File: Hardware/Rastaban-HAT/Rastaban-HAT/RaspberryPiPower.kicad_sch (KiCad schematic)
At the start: 11 parts, among them IC2 BCM53DS, Q3 DMG2305UX-7, U5 LM2596S -5.0

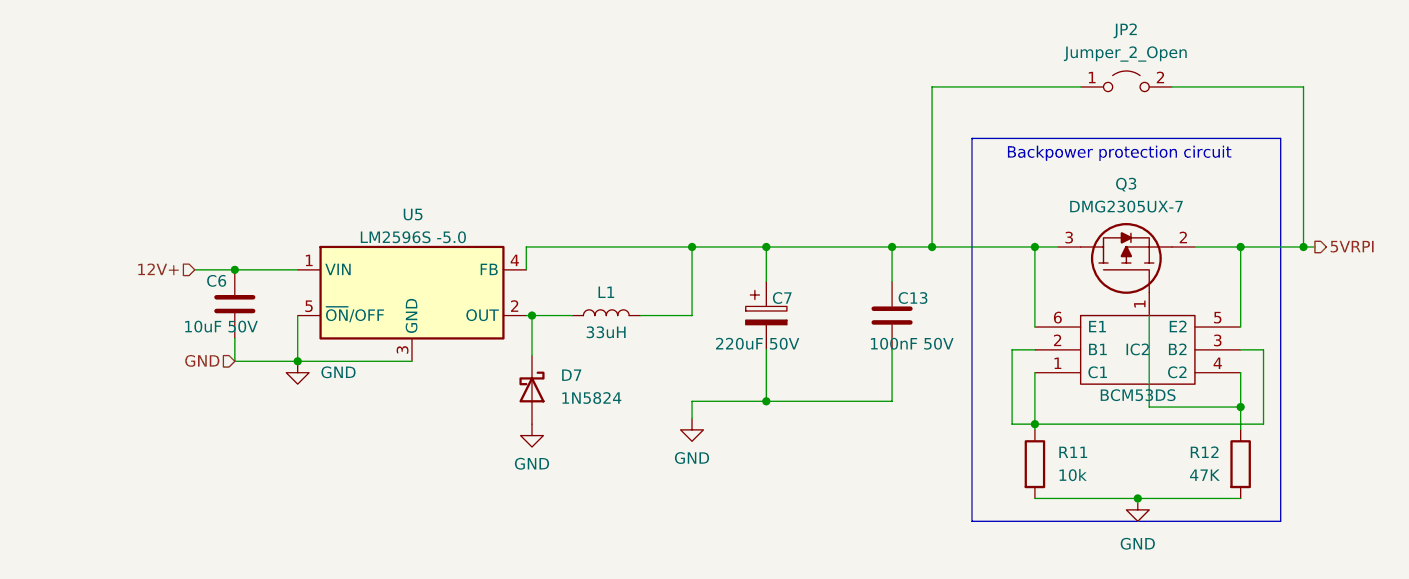
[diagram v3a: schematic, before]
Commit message: improved RPI Power circuit
-added capacitors and values
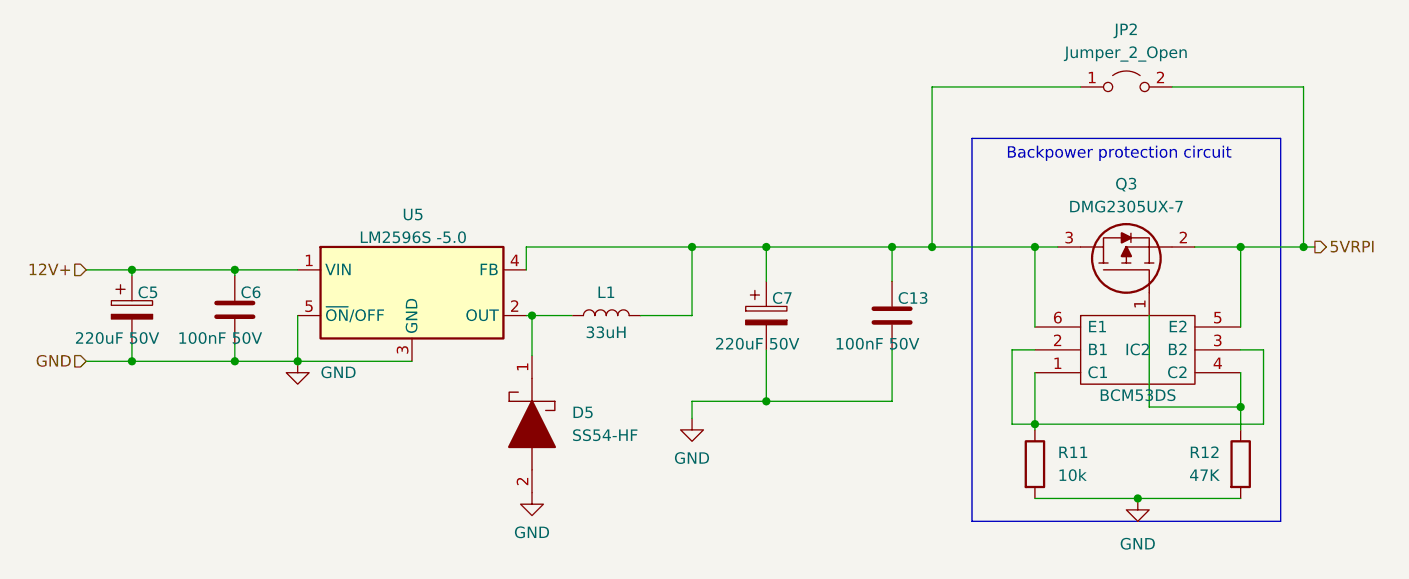
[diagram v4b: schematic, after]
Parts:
- removed D7: 1N5824, SamacSys_Parts:SOD2512X110N, symbol Device:D_Schottky
- added C5: 220uF 50V, Capacitor_SMD:CP_Elec_8x10, symbol Device:C_Polarized
- added D5: SS54-HF, DIOM5025X220N, symbol SamacSys_Parts:SS54-HF
- C6: value 10uF 50V -> 100nF 50V
- L1: footprint Inductor_SMD:L_Bourns-SRU8028_8.0x8.0mm -> Inductor_SMD:L_Bourns_SRR1208_12.7x12.7mm
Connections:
- net 12V+: now also C5.1
- net GND: now also C5.2, D5.2
- net at L1.1, U5.2 (OUT): now also D5.1
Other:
- moved on the sheet: C6
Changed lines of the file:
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@@
   (junction (at 50.165 60.96) (diameter 0) (color 0 0 0 0)
   )
+  (junction (at 38.735 60.96) (diameter 0) (color 0 0 0 0)
+  )
   (junction (at 100.965 58.42) (diameter 0) (color 0 0 0 0)
   )
@@
   (junction (at 127.635 58.42) (diameter 0) (color 0 0 0 0)
   )
+  (junction (at 50.165 71.12) (diameter 0) (color 0 0 0 0)
+  )
   (junction (at 83.185 66.04) (diameter 0) (color 0 0 0 0)
   )
+  (junction (at 38.735 71.12) (diameter 0) (color 0 0 0 0)
+  )
   (junction (at 109.22 58.42) (diameter 0) (color 0 0 0 0)
   )
@@
     (stroke (width 0) (type default) (color 0 0 0 0))
   )
-  (wire (pts (xy 50.165 68.58) (xy 50.165 71.12))
+  (wire (pts (xy 50.165 69.215) (xy 50.165 71.12))
     (stroke (width 0) (type default) (color 0 0 0 0))
   )
@@
     (stroke (width 0) (type default) (color 0 0 0 0))
   )
+  (wire (pts (xy 50.165 61.595) (xy 50.165 60.96))
+    (stroke (width 0) (type default) (color 0 0 0 0))
+  )
   (wire (pts (xy 139.065 58.42) (xy 139.065 67.31))
     (stroke (width 0) (type default) (color 0 0 0 0))
@@
     (stroke (width 0) (type default) (color 0 0 0 0))
   )
+  (wire (pts (xy 38.735 69.215) (xy 38.735 71.12))
+    (stroke (width 0) (type default) (color 0 0 0 0))
+  )
   (wire (pts (xy 127.635 40.64) (xy 127.635 58.42))
     (stroke (width 0) (type default) (color 0 0 0 0))
@@
     (stroke (width 0) (type default) (color 0 0 0 0))
   )
+  (wire (pts (xy 38.735 71.12) (xy 50.165 71.12))
+    (stroke (width 0) (type default) (color 0 0 0 0))
+  )
   (wire (pts (xy 109.22 69.85) (xy 109.22 75.565))
     (stroke (width 0) (type default) (color 0 0 0 0))
@@
     (stroke (width 0) (type default) (color 0 0 0 0))
   )
-  (wire (pts (xy 45.72 60.96) (xy 50.165 60.96))
+  (wire (pts (xy 38.735 60.96) (xy 50.165 60.96))
+    (stroke (width 0) (type default) (color 0 0 0 0))
+  )
+  (wire (pts (xy 33.655 60.96) (xy 38.735 60.96))
     (stroke (width 0) (type default) (color 0 0 0 0))
   )
   (wire (pts (xy 161.925 69.85) (xy 164.465 69.85))
+    (stroke (width 0) (type default) (color 0 0 0 0))
+  )
+  (wire (pts (xy 33.655 71.12) (xy 38.735 71.12))
+    (stroke (width 0) (type default) (color 0 0 0 0))
+  )
+  (wire (pts (xy 38.735 61.595) (xy 38.735 60.96))
     (stroke (width 0) (type default) (color 0 0 0 0))
   )
@@
     (effects (font (size 1.27 1.27)) (justify left))
   )
-  (hierarchical_label "12V+" (shape input) (at 45.72 60.96 180)
+  (hierarchical_label "12V+" (shape input) (at 33.655 60.96 180)
     (effects (font (size 1.27 1.27)) (justify right))
   )
-  (hierarchical_label "GND" (shape input) (at 50.165 71.12 180)
+  (hierarchical_label "GND" (shape input) (at 33.655 71.12 180)
     (effects (font (size 1.27 1.27)) (justify right))
   )
-  (symbol (lib_id "power:GND") (at 83.185 78.105 0) (unit 1)
-    (in_bom yes) (on_board yes) (fields_autoplaced)
-    (property "Reference" "#PWR0105" (id 0) (at 83.185 84.455 0)
-      (effects (font (size 1.27 1.27)) hide)
-    )
-    (property "Value" "GND" (id 1) (at 83.185 82.5484 0))
-    (property "Footprint" "" (id 2) (at 83.185 78.105 0)
-      (effects (font (size 1.27 1.27)) hide)
-    )
-    (property "Datasheet" "" (id 3) (at 83.185 78.105 0)
+  (symbol (lib_id "power:GND") (at 83.185 85.725 0) (unit 1)
+    (in_bom yes) (on_board yes) (fields_autoplaced)
+    (property "Reference" "#PWR0105" (id 0) (at 83.185 92.075 0)
+      (effects (font (size 1.27 1.27)) hide)
+    )
+    (property "Value" "GND" (id 1) (at 83.185 90.1684 0))
+    (property "Footprint" "" (id 2) (at 83.185 85.725 0)
+      (effects (font (size 1.27 1.27)) hide)
+    )
+    (property "Datasheet" "" (id 3) (at 83.185 85.725 0)
       (effects (font (size 1.27 1.27)) hide)
     )
@@
     (pin "2")
   )
-  (symbol (lib_id "Device:C") (at 50.165 64.77 0) (unit 1)
-    (in_bom yes) (on_board yes)
-    (property "Reference" "C6" (id 0) (at 46.99 62.23 0)
-      (effects (font (size 1.27 1.27)) (justify left))
-    )
-    (property "Value" "10uF 50V" (id 1) (at 44.45 67.31 0)
-      (effects (font (size 1.27 1.27)) (justify left))
-    )
-    (property "Footprint" "Capacitor_SMD:C_0805_2012Metric_Pad1.18x1.45mm_HandSolder" (id 2) (at 51.1302 68.58 0)
-      (effects (font (size 1.27 1.27)) hide)
-    )
-    (property "Datasheet" "~" (id 3) (at 50.165 64.77 0)
-      (effects (font (size 1.27 1.27)) hide)
-    )
-    (property "LCSC" "C15850" (id 4) (at 50.165 64.77 0)
+  (symbol (lib_id "Device:C") (at 50.165 65.405 0) (unit 1)
+    (in_bom yes) (on_board yes)
+    (property "Reference" "C6" (id 0) (at 50.8 63.5 0)
+      (effects (font (size 1.27 1.27)) (justify left))
+    )
+    (property "Value" "100nF 50V" (id 1) (at 43.815 68.58 0)
+      (effects (font (size 1.27 1.27)) (justify left))
+    )
+    (property "Footprint" "Capacitor_SMD:C_0805_2012Metric_Pad1.18x1.45mm_HandSolder" (id 2) (at 51.1302 69.215 0)
+      (effects (font (size 1.27 1.27)) hide)
+    )
+    (property "Datasheet" "~" (id 3) (at 50.165 65.405 0)
+      (effects (font (size 1.27 1.27)) hide)
+    )
+    (property "LCSC" "C15850" (id 4) (at 50.165 65.405 0)
       (effects (font (size 1.27 1.27)) hide)
     )
@@
       (effects (font (size 1.27 1.27)) (justify right))
     )
-    (property "Value" "100nF 50V" (id 1) (at 120.65 69.215 0)
+    (property "Value" "100nF 50V" (id 1) (at 116.84 69.215 0)
       (effects (font (size 1.27 1.27)) (justify right))
     )
@@
     )
     (pin "1")
-  )
-  (symbol (lib_id "Device:D_Schottky") (at 83.185 74.295 270) (unit 1)
-    (in_bom yes) (on_board yes) (fields_autoplaced)
-    (property "Reference" "D7" (id 0) (at 86.36 72.7074 90)
-      (effects (font (size 1.27 1.27)) (justify left))
-    )
-    (property "Value" "1N5824" (id 1) (at 86.36 75.2474 90)
-      (effects (font (size 1.27 1.27)) (justify left))
-    )
-    (property "Footprint" "SamacSys_Parts:SOD2512X110N" (id 2) (at 83.185 74.295 0)
-      (effects (font (size 1.27 1.27)) hide)
-    )
-    (property "Datasheet" "~" (id 3) (at 83.185 74.295 0)
-      (effects (font (size 1.27 1.27)) hide)
-    )
-    (pin "1")
-    (pin "2")
   )
   (symbol (lib_id "Regulator_Switching:LM2596S-ADJ") (at 69.85 63.5 0) (unit 1)
@@
     (property "Reference" "L1" (id 0) (at 91.44 63.5 90))
     (property "Value" "33uH" (id 1) (at 91.44 67.945 90))
-    (property "Footprint" "Inductor_SMD:L_Bourns-SRU8028_8.0x8.0mm" (id 2) (at 91.44 66.04 0)
+    (property "Footprint" "Inductor_SMD:L_Bourns_SRR1208_12.7x12.7mm" (id 2) (at 91.44 66.04 0)
       (effects (font (size 1.27 1.27)) hide)
     )
@@
     )
     (property "LCSC" "C82571" (id 5) (at 91.44 66.04 90)
+      (effects (font (size 1.27 1.27)) hide)
+    )
+    (pin "1")
+    (pin "2")
+  )
+  (symbol (lib_id "Device:C_Polarized") (at 38.735 65.405 0) (unit 1)
+    (in_bom yes) (on_board yes)
+    (property "Reference" "C5" (id 0) (at 39.37 63.5 0)
+      (effects (font (size 1.27 1.27)) (justify left))
+    )
+    (property "Value" "220uF 50V" (id 1) (at 32.385 68.58 0)
+      (effects (font (size 1.27 1.27)) (justify left))
+    )
+    (property "Footprint" "Capacitor_SMD:CP_Elec_8x10" (id 2) (at 39.7002 69.215 0)
+      (effects (font (size 1.27 1.27)) hide)
+    )
+    (property "Datasheet" "~" (id 3) (at 38.735 65.405 0)
+      (effects (font (size 1.27 1.27)) hide)
+    )
+    (property "LCSC Part#" "" (id 4) (at 38.735 65.405 0)
+      (effects (font (size 1.27 1.27)) hide)
+    )
+    (property "Manufacturer_Part_Number" "C3339" (id 5) (at 38.735 65.405 0)
+      (effects (font (size 1.27 1.27)) hide)
+    )
+    (property "Purpose" "decoupling" (id 6) (at 38.735 65.405 0)
+      (effects (font (size 1.27 1.27)) hide)
+    )
+    (property "LCSC" "C445063" (id 7) (at 38.735 65.405 0)
       (effects (font (size 1.27 1.27)) hide)
     )
@@
     (pin "6")
   )
+  (symbol (lib_id "SamacSys_Parts:SS54-HF") (at 83.185 67.945 270) (unit 1)
+    (in_bom yes) (on_board yes) (fields_autoplaced)
+    (property "Reference" "D5" (id 0) (at 87.63 76.8349 90)
+      (effects (font (size 1.27 1.27)) (justify left))
+    )
+    (property "Value" "SS54-HF" (id 1) (at 87.63 79.3749 90)
+      (effects (font (size 1.27 1.27)) (justify left))
+    )
+    (property "Footprint" "DIOM5025X220N" (id 2) (at 86.995 80.645 0)
+      (effects (font (size 1.27 1.27)) (justify left) hide)
+    )
+    (property "Datasheet" "https://componentsearchengine.com/Datasheets/1/SS54-HF.pdf" (id 3) (at 84.455 80.645 0)
+      (effects (font (size 1.27 1.27)) (justify left) hide)
+    )
+    (property "Description" "DIODE SCHOTTKY 5A 40V SMA" (id 4) (at 81.915 80.645 0)
+      (effects (font (size 1.27 1.27)) (justify left) hide)
+    )
+    (property "Height" "2.2" (id 5) (at 79.375 80.645 0)
+      (effects (font (size 1.27 1.27)) (justify left) hide)
+    )
+    (property "Mouser Part Number" "750-SS54-HF" (id 6) (at 76.835 80.645 0)
+      (effects (font (size 1.27 1.27)) (justify left) hide)
+    )
+    (property "Mouser Price/Stock" "https://www.mouser.co.uk/ProductDetail/Comchip-Technology/SS54-HF?qs=GBLSl2AkiruU27AsKMcmrg%3D%3D" (id 7) (at 74.295 80.645 0)
+      (effects (font (size 1.27 1.27)) (justify left) hide)
+    )
+    (property "Manufacturer_Name" "Comchip Technology" (id 8) (at 71.755 80.645 0)
+      (effects (font (size 1.27 1.27)) (justify left) hide)
+    )
+    (property "Manufacturer_Part_Number" "SS54-HF" (id 9) (at 69.215 80.645 0)
+      (effects (font (size 1.27 1.27)) (justify left) hide)
+    )
+    (pin "1")
+    (pin "2")
+  )
 )

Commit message: added tmc2208 footprints to 2209 schematic symbol
interchangable since the TMC drivers have roughly the same pinout.
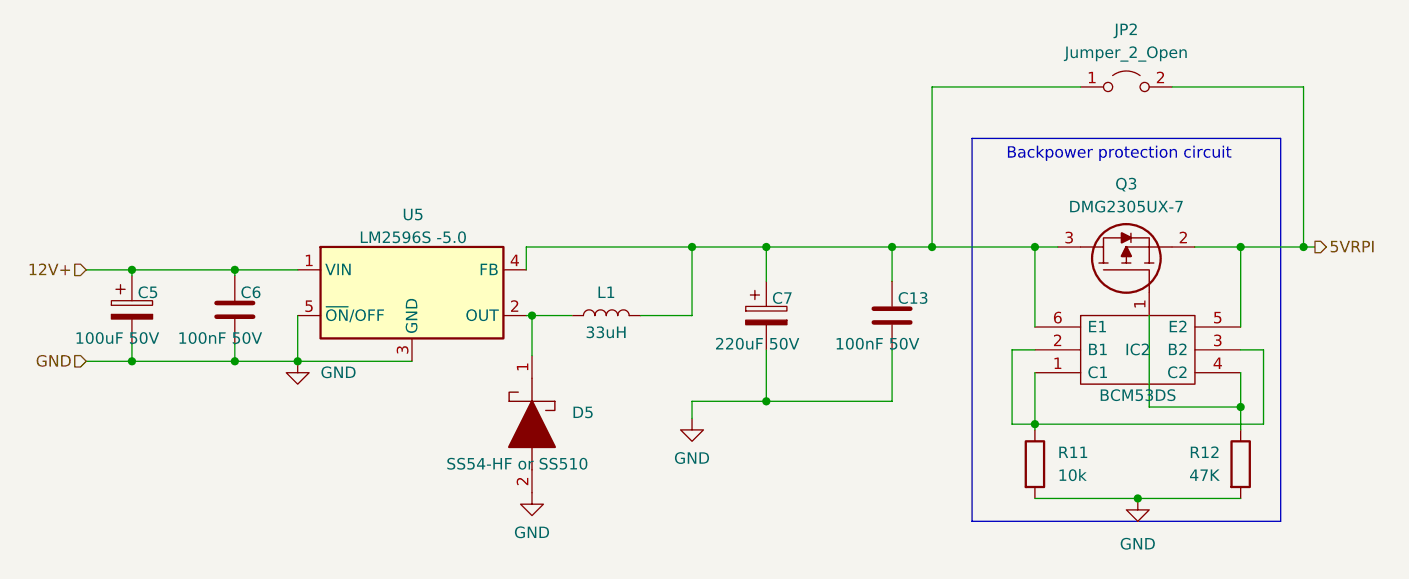
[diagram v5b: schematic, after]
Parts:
- C5: value 220uF 50V -> 100uF 50V
- D5: value SS54-HF -> SS54-HF or SS510; footprint DIOM5025X220N -> SamacSys_Parts:DIOM5025X220N
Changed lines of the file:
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@@
       (effects (font (size 1.27 1.27)) (justify left))
     )
-    (property "Value" "220uF 50V" (id 1) (at 32.385 68.58 0)
+    (property "Value" "100uF 50V" (id 1) (at 32.385 68.58 0)
       (effects (font (size 1.27 1.27)) (justify left))
     )
@@
   )
   (symbol (lib_id "SamacSys_Parts:SS54-HF") (at 83.185 67.945 270) (unit 1)
-    (in_bom yes) (on_board yes) (fields_autoplaced)
+    (in_bom yes) (on_board yes)
     (property "Reference" "D5" (id 0) (at 87.63 76.8349 90)
       (effects (font (size 1.27 1.27)) (justify left))
     )
-    (property "Value" "SS54-HF" (id 1) (at 87.63 79.3749 90)
+    (property "Value" "SS54-HF or SS510" (id 1) (at 73.66 82.55 90)
       (effects (font (size 1.27 1.27)) (justify left))
     )
-    (property "Footprint" "DIOM5025X220N" (id 2) (at 86.995 80.645 0)
+    (property "Footprint" "SamacSys_Parts:DIOM5025X220N" (id 2) (at 86.995 80.645 0)
       (effects (font (size 1.27 1.27)) (justify left) hide)
     )

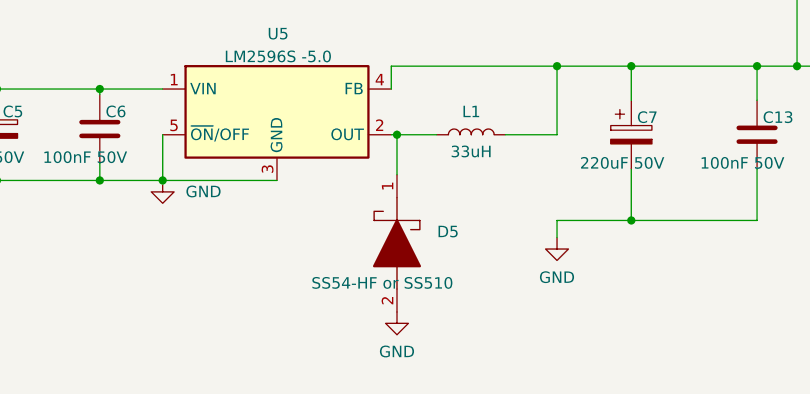
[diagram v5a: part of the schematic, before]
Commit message: NEW led driver circuit added
CN5711 added.
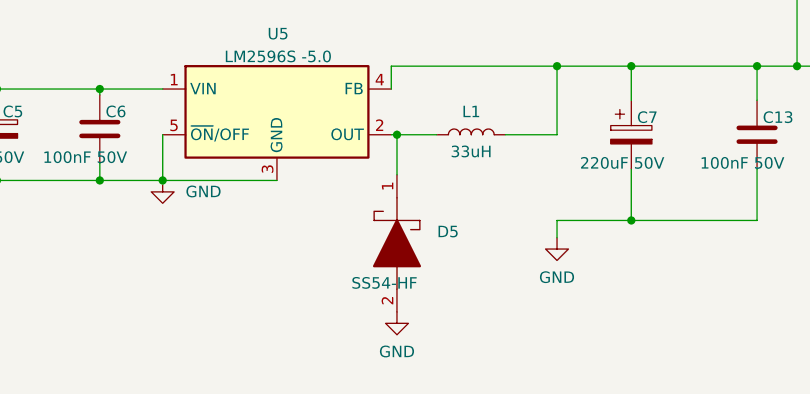
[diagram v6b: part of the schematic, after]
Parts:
- D5: value SS54-HF or SS510 -> SS54-HF; Note (none) -> SS510 also suitable
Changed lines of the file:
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@@
       (effects (font (size 1.27 1.27)) (justify left))
     )
-    (property "Value" "SS54-HF or SS510" (id 1) (at 73.66 82.55 90)
+    (property "Value" "SS54-HF " (id 1) (at 78.105 82.55 90)
       (effects (font (size 1.27 1.27)) (justify left))
     )
@@
       (effects (font (size 1.27 1.27)) (justify left) hide)
     )
+    (property "Note" "SS510 also suitable" (id 11) (at 83.185 67.945 90)
+      (effects (font (size 1.27 1.27)) hide)
+    )
     (pin "1")

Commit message: changed capacitor footprints
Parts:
- C13: footprint Capacitor_SMD:C_1206_3216Metric_Pad1.33x1.80mm_HandSolder -> Capacitor_SMD:C_0805_2012Metric_Pad1.18x1.45mm_HandSolder
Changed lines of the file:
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@@
       (effects (font (size 1.27 1.27)) (justify right))
     )
-    (property "Footprint" "Capacitor_SMD:C_1206_3216Metric_Pad1.33x1.80mm_HandSolder" (id 2) (at 122.2248 62.23 0)
+    (property "Footprint" "Capacitor_SMD:C_0805_2012Metric_Pad1.18x1.45mm_HandSolder" (id 2) (at 122.2248 62.23 0)
       (effects (font (size 1.27 1.27)) hide)
     )
